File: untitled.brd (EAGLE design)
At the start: 54.8 x 54.7 mm, 25 parts

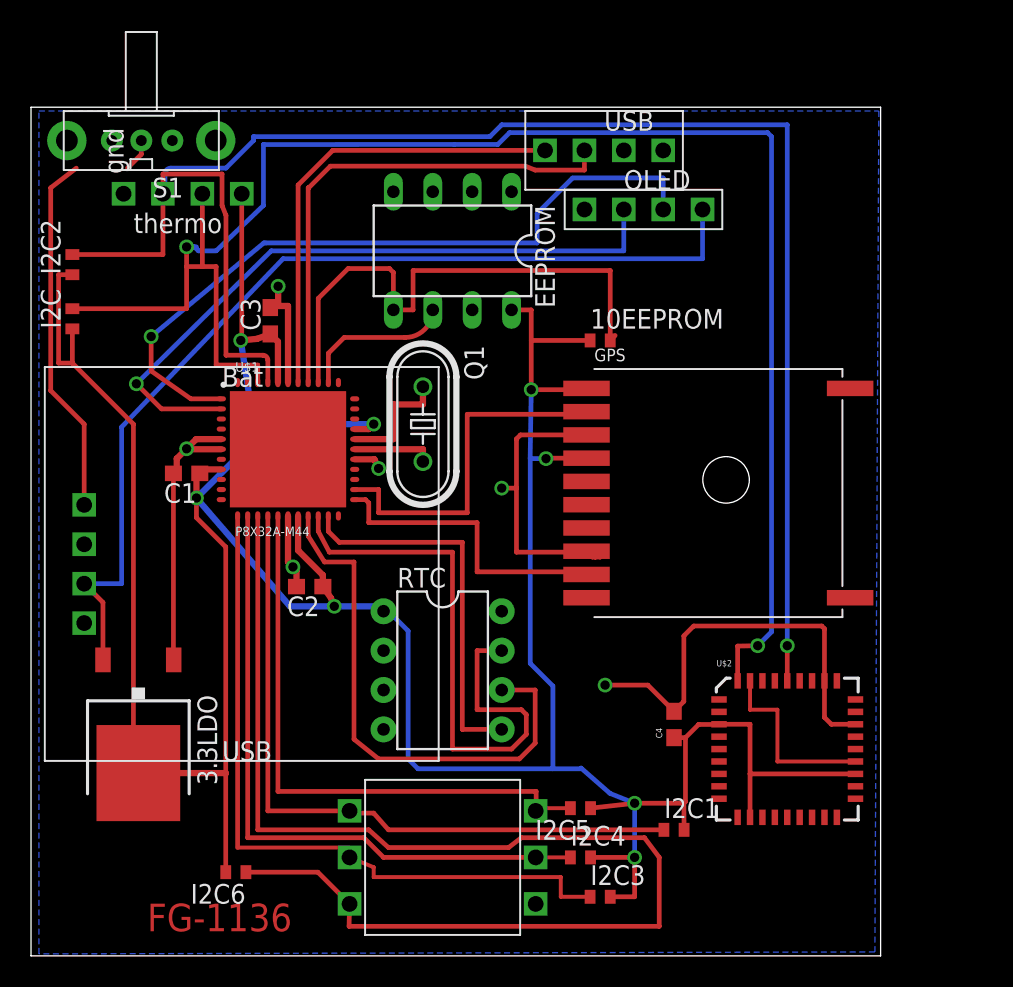
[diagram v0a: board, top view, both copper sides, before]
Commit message: added optional speaker
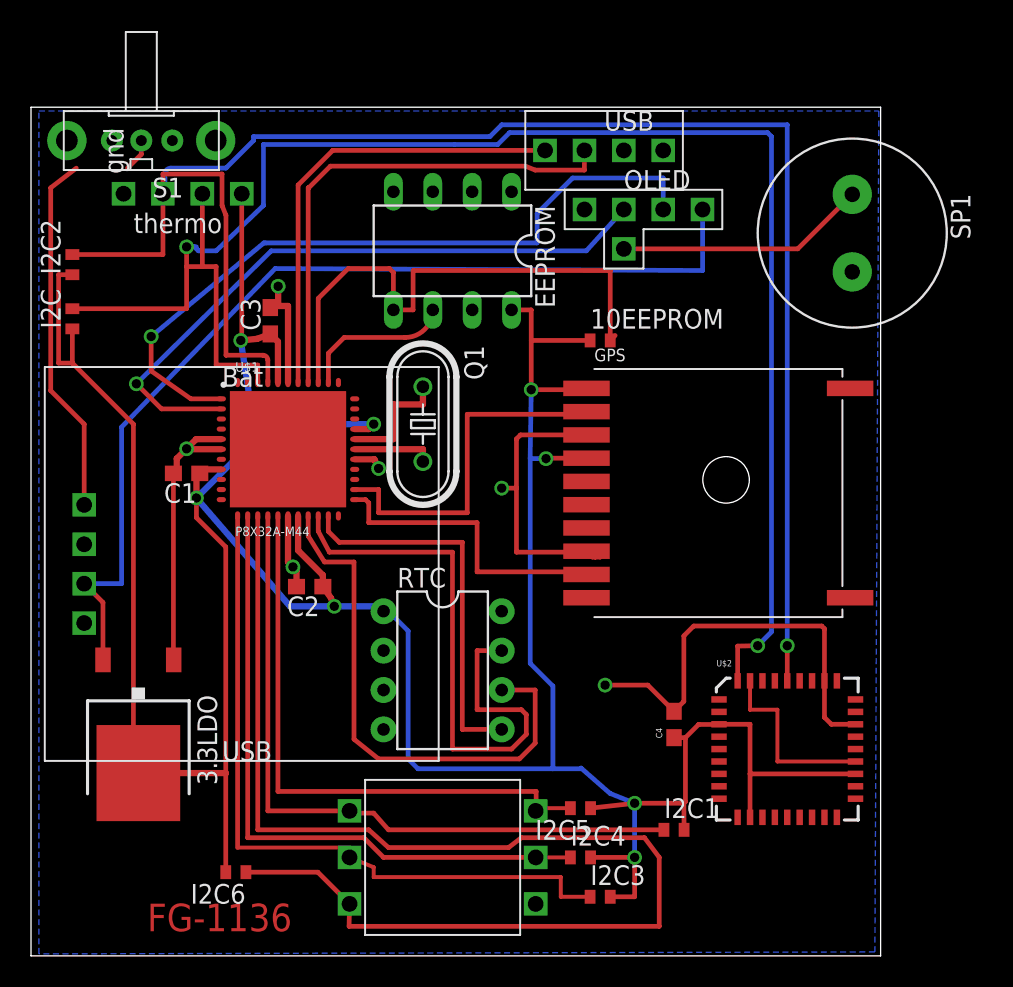
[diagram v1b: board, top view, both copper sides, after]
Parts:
- added SP1: SPEAKER/PS12, adafruit:PS12
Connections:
- new net N$12: OLED_SCREEN.PEZ, SP1.P$1
- net GND: now also SP1.P$2
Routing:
- net N$12: track 0.00 -> 16.2 mm
- net N$10: track 43.8 -> 42.3 mm
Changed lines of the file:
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@@
 <element name="C4" library="SparkFun" package="0603" value="" x="79.6925" y="25.0825" rot="R90"/>
 <element name="3.3LDO" library="burr-brown" package="TO252" value="REG1117X" x="45.1485" y="24.4475" rot="R180"/>
+<element name="SP1" library="adafruit" package="PS12" value="SPEAKER/PS12" x="91.186" y="56.769" rot="R270"/>
 </elements>
 <signals>
@@
 <wire x1="46.6437" y1="45.4313" x2="45.0215" y2="47.0535" width="0.3048" layer="1"/>
 <wire x1="45.0215" y1="47.0535" x2="53.721" y2="55.626" width="0.3048" layer="16"/>
-<wire x1="53.721" y1="55.626" x2="76.454" y2="55.626" width="0.3048" layer="16"/>
-<wire x1="76.454" y1="58.293" x2="76.454" y2="55.626" width="0.3048" layer="16"/>
+<wire x1="53.721" y1="55.626" x2="74.041" y2="55.626" width="0.3048" layer="16"/>
+<wire x1="74.041" y1="55.626" x2="76.454" y2="58.293" width="0.3048" layer="16"/>
 </signal>
 <signal name="N$11">
@@
 <wire x1="47.4285" y1="29.2475" x2="47.41" y2="29.2475" width="0.3048" layer="1"/>
 <wire x1="47.41" y1="29.2475" x2="47.41" y2="41.275" width="0.3048" layer="1"/>
+<contactref element="SP1" pad="P$2"/>
 </signal>
 <signal name="+5V">
@@
 <contactref element="OLED_SCREEN" pad="5V"/>
 <contactref element="3.3LDO" pad="2"/>
-<wire x1="81.534" y1="55.118" x2="54.483" y2="55.118" width="0.3048" layer="16"/>
+<wire x1="81.534" y1="54.356" x2="53.975" y2="54.483" width="0.3048" layer="16"/>
 <wire x1="41.656" y1="34.163" x2="42.8685" y2="32.9505" width="0.3048" layer="1"/>
 <wire x1="42.8685" y1="32.9505" x2="42.8685" y2="29.2475" width="0.3048" layer="1"/>
 <wire x1="44.069" y1="44.2595" x2="44.069" y2="34.163" width="0.3048" layer="16"/>
 <wire x1="44.069" y1="34.163" x2="41.656" y2="34.163" width="0.3048" layer="16"/>
-<wire x1="81.534" y1="58.293" x2="81.534" y2="55.118" width="0.3048" layer="16"/>
-<wire x1="54.483" y1="55.118" x2="44.069" y2="44.2595" width="0.3048" layer="16"/>
+<wire x1="81.534" y1="58.293" x2="81.534" y2="54.356" width="0.3048" layer="16"/>
+<wire x1="53.975" y1="54.483" x2="44.069" y2="44.2595" width="0.3048" layer="16"/>
 </signal>
 <signal name="+3V3">
@@
 <wire x1="70.485" y1="51.816" x2="70.485" y2="49.8475" width="0.3048" layer="1"/>
 </signal>
+<signal name="N$12">
+<contactref element="OLED_SCREEN" pad="PEZ"/>
+<contactref element="SP1" pad="P$1"/>
+<wire x1="91.186" y1="59.269" x2="87.67" y2="55.753" width="0.3048" layer="1"/>
+<wire x1="87.67" y1="55.753" x2="76.454" y2="55.753" width="0.3048" layer="1"/>
+</signal>
 </signals>

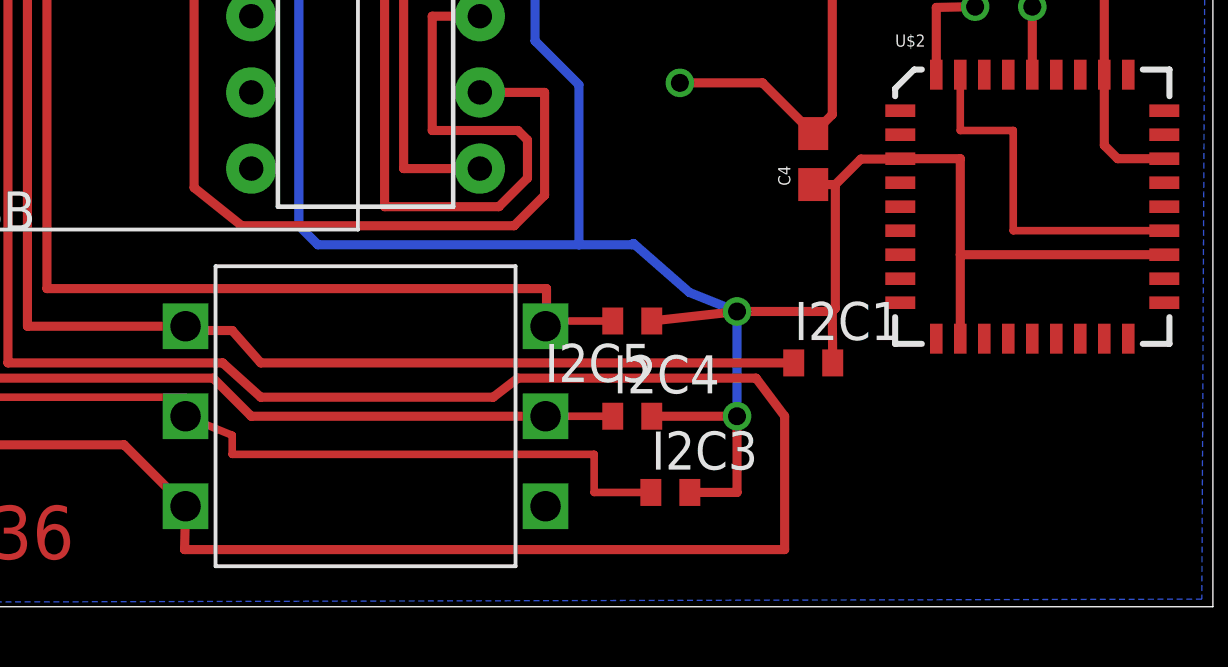
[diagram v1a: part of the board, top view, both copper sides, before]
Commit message: moved switch resistors to better fit 3d case.
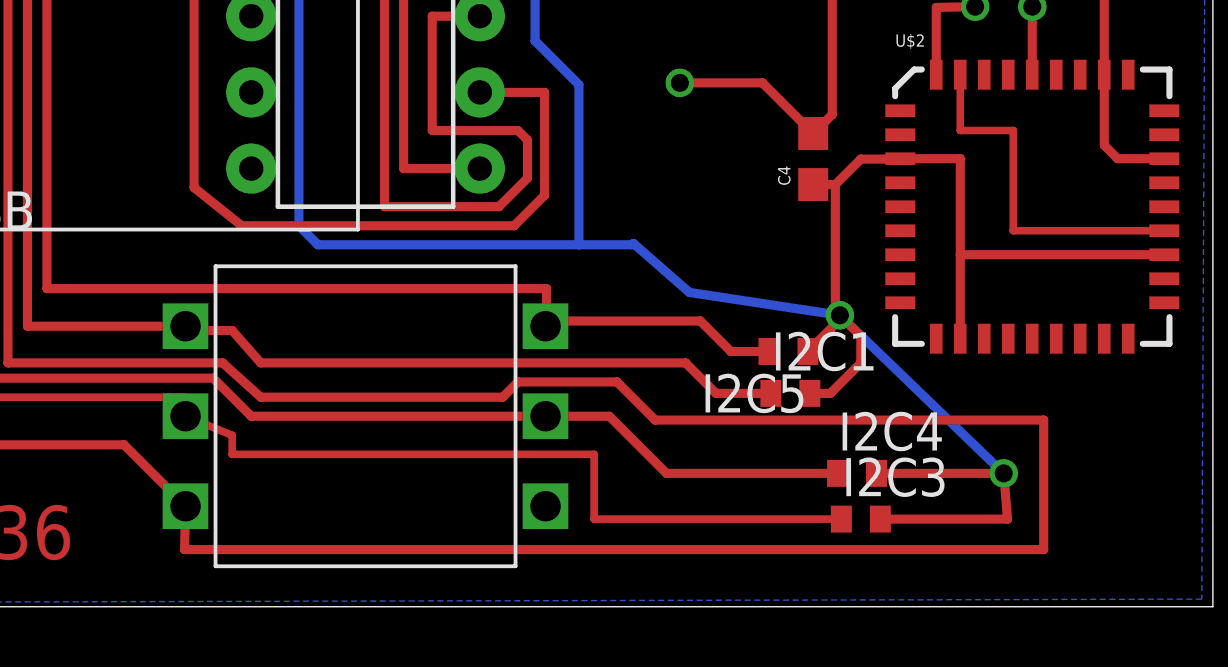
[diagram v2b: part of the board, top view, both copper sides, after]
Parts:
- moved I2C4 7.73 mm to (81.2, 14.6)
- moved I2C3 6.41 mm to (81.3, 13.1)
- moved I2C5 5.31 mm to (78.9, 18.7)
- moved I2C1 1.27 mm to (78.9, 17.3)
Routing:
- net N$15: track 80.8 -> 97.9 mm
- net +3V3: track 238.8 -> 247.4 mm
- net N$20: track 42.1 -> 50.4 mm
- net N$17: track 46.8 -> 54.0 mm
- net N$21: track 38.1 -> 43.7 mm
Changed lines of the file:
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@@
 <element name="I2C2" library="adafruit" package="R1005" value="" x="40.894" y="54.737" rot="R90"/>
 <element name="I2C" library="adafruit" package="R1005" value="" x="40.894" y="51.2445" rot="R90"/>
-<element name="I2C5" library="adafruit" package="R1005" value="" x="73.66" y="19.685" rot="R180"/>
-<element name="I2C4" library="adafruit" package="R1005" value="" x="73.66" y="16.51"/>
-<element name="I2C3" library="adafruit" package="R1005" value="" x="74.93" y="13.97"/>
+<element name="I2C5" library="adafruit" package="R1005" value="" x="78.867" y="18.669" rot="R180"/>
+<element name="I2C4" library="adafruit" package="R1005" value="" x="81.153" y="14.605"/>
+<element name="I2C3" library="adafruit" package="R1005" value="" x="81.28" y="13.081"/>
 <element name="I2C6" library="adafruit" package="R1005" value="" x="51.435" y="15.5575" rot="R180"/>
-<element name="I2C1" library="adafruit" package="R1005" value="" x="79.6925" y="18.288"/>
+<element name="I2C1" library="adafruit" package="R1005" value="" x="78.9305" y="17.272"/>
 <element name="U$2" library="SparkFun" package="LCC36" value="HMC6343A" x="86.995" y="23.495"/>
 <element name="C1" library="rcl" package="C0603" value="" x="48.26" y="41.275" rot="R180"/>
@@
 <wire x1="53.5" y1="38.5313" x2="53.5" y2="19.51" width="0.3048" layer="1"/>
 <wire x1="53.5" y1="19.51" x2="58.77" y2="19.51" width="0.3048" layer="1"/>
-<wire x1="79.0425" y1="18.288" x2="61.2775" y2="18.288" width="0.3048" layer="1"/>
 <wire x1="61.2775" y1="18.288" x2="60.325" y2="19.3675" width="0.3048" layer="1"/>
 <wire x1="60.325" y1="19.3675" x2="58.9125" y2="19.3675" width="0.3048" layer="1"/>
 <wire x1="58.9125" y1="19.3675" x2="58.77" y2="19.51" width="0.3048" layer="1"/>
+<wire x1="78.2805" y1="17.272" x2="76.454" y2="17.272" width="0.3048" layer="1"/>
+<wire x1="75.438" y1="18.288" x2="61.2775" y2="18.288" width="0.3048" layer="1"/>
+<wire x1="75.438" y1="18.288" x2="76.454" y2="17.272" width="0.3048" layer="1"/>
 </signal>
 <signal name="N$15">
@@
 <contactref element="I2C6" pad="1"/>
 <wire x1="52.85" y1="38.5313" x2="52.85" y2="18.288" width="0.3048" layer="1"/>
-<wire x1="77.7875" y1="17.78" x2="78.74" y2="16.51" width="0.3048" layer="1"/>
-<wire x1="78.74" y1="16.51" x2="78.74" y2="12.065" width="0.3048" layer="1"/>
-<wire x1="78.74" y1="12.065" x2="58.7375" y2="12.065" width="0.3048" layer="1"/>
+<wire x1="87.376" y1="16.383" x2="87.376" y2="12.065" width="0.3048" layer="1"/>
+<wire x1="87.376" y1="12.065" x2="58.7375" y2="12.065" width="0.3048" layer="1"/>
 <wire x1="58.7375" y1="12.065" x2="58.77" y2="13.51" width="0.3048" layer="1"/>
 <wire x1="52.85" y1="18.288" x2="60.0075" y2="18.288" width="0.3048" layer="1"/>
 <wire x1="60.0075" y1="18.288" x2="61.2775" y2="17.145" width="0.3048" layer="1"/>
-<wire x1="61.2775" y1="17.145" x2="69.0245" y2="17.145" width="0.3048" layer="1"/>
-<wire x1="69.85" y1="17.78" x2="77.7875" y2="17.78" width="0.3048" layer="1"/>
 <wire x1="52.085" y1="15.5575" x2="56.7225" y2="15.5575" width="0.3048" layer="1"/>
 <wire x1="56.7225" y1="15.5575" x2="58.77" y2="13.51" width="0.3048" layer="1"/>
-<wire x1="69.85" y1="17.78" x2="69.0245" y2="17.145" width="0.3048" layer="1"/>
+<wire x1="61.2775" y1="17.145" x2="69.342" y2="17.145" width="0.3048" layer="1"/>
+<wire x1="69.342" y1="17.145" x2="69.85" y2="17.653" width="0.3048" layer="1"/>
+<wire x1="69.85" y1="17.653" x2="73.152" y2="17.653" width="0.3048" layer="1"/>
+<wire x1="74.422" y1="16.383" x2="87.376" y2="16.383" width="0.3048" layer="1"/>
+<wire x1="73.152" y1="17.653" x2="74.422" y2="16.383" width="0.3048" layer="1"/>
 </signal>
 <signal name="N$17">
@@
 <contactref element="U$1" pad="12"/>
 <contactref element="5WAYSWITCH" pad="L"/>
-<wire x1="74.28" y1="13.97" x2="72.39" y2="13.97" width="0.254" layer="1"/>
-<wire x1="72.39" y1="13.97" x2="72.39" y2="15.24" width="0.254" layer="1"/>
+<wire x1="80.63" y1="13.081" x2="72.39" y2="13.081" width="0.254" layer="1"/>
+<wire x1="72.39" y1="13.081" x2="72.39" y2="15.24" width="0.254" layer="1"/>
 <wire x1="72.39" y1="15.24" x2="60.325" y2="15.24" width="0.254" layer="1"/>
 <wire x1="60.325" y1="15.24" x2="60.325" y2="15.875" width="0.254" layer="1"/>
@@
 <contactref element="I2C4" pad="1"/>
 <contactref element="U$1" pad="13"/>
-<wire x1="73.01" y1="16.51" x2="70.77" y2="16.51" width="0.254" layer="1"/>
 <wire x1="52.2" y1="38.5313" x2="52.2" y2="17.78" width="0.3048" layer="1"/>
 <wire x1="70.8025" y1="16.51" x2="70.77" y2="16.51" width="0.3048" layer="1"/>
@@
 <wire x1="59.69" y1="17.78" x2="60.96" y2="16.51" width="0.3048" layer="1"/>
 <wire x1="60.96" y1="16.51" x2="70.77" y2="16.51" width="0.3048" layer="1"/>
+<wire x1="74.803" y1="14.605" x2="80.503" y2="14.605" width="0.3048" layer="1"/>
+<wire x1="70.77" y1="16.51" x2="72.898" y2="16.51" width="0.3048" layer="1"/>
+<wire x1="72.898" y1="16.51" x2="74.803" y2="14.605" width="0.3048" layer="1"/>
 </signal>
 <signal name="N$21">
@@
 <contactref element="U$1" pad="16"/>
 <contactref element="I2C5" pad="2"/>
-<wire x1="73.01" y1="19.685" x2="70.77" y2="19.685" width="0.254" layer="1"/>
 <wire x1="70.77" y1="19.685" x2="70.77" y2="19.51" width="0.254" layer="1"/>
 <wire x1="54.15" y1="38.5313" x2="54.15" y2="20.7645" width="0.3048" layer="1"/>
@@
 <wire x1="70.8025" y1="20.7645" x2="70.8025" y2="19.51" width="0.3048" layer="1"/>
 <wire x1="70.8025" y1="19.51" x2="70.77" y2="19.51" width="0.3048" layer="1"/>
+<wire x1="70.77" y1="19.685" x2="75.931" y2="19.685" width="0.3048" layer="1"/>
+<wire x1="75.931" y1="19.685" x2="76.947" y2="18.669" width="0.3048" layer="1"/>
+<wire x1="76.947" y1="18.669" x2="78.217" y2="18.669" width="0.3048" layer="1"/>
 </signal>
 <signal name="N$22">
@@
 <wire x1="60.96" y1="32.7025" x2="57.785" y2="32.7025" width="0.4064" layer="16"/>
 <wire x1="73.6993375" y1="22.26995625" x2="75.565" y2="20.6375" width="0.3048" layer="16"/>
-<wire x1="75.565" y1="20.6375" x2="77.1525" y2="20.0025" width="0.3048" layer="16"/>
-<wire x1="77.1525" y1="20.0025" x2="77.1525" y2="16.51" width="0.3048" layer="16"/>
-<via x="77.1525" y="16.51" extent="1-16" drill="0.6" shape="square"/>
-<wire x1="77.1525" y1="16.51" x2="74.31" y2="16.51" width="0.3048" layer="1"/>
-<via x="77.1525" y="20.0025" extent="1-16" drill="0.6" shape="square"/>
-<wire x1="77.1525" y1="20.0025" x2="74.31" y2="19.685" width="0.3048" layer="1"/>
-<wire x1="75.58" y1="13.97" x2="77.1525" y2="13.97" width="0.3048" layer="1"/>
-<wire x1="77.1525" y1="13.97" x2="77.1525" y2="16.51" width="0.3048" layer="1"/>
-<wire x1="77.1525" y1="20.0025" x2="80.3275" y2="20.0025" width="0.3048" layer="1"/>
-<wire x1="80.3275" y1="20.0025" x2="80.3425" y2="18.288" width="0.3048" layer="1"/>
+<wire x1="75.565" y1="20.6375" x2="80.5815" y2="19.8755" width="0.3048" layer="16"/>
+<wire x1="80.5815" y1="19.8755" x2="86.0425" y2="14.605" width="0.3048" layer="16"/>
+<via x="86.0425" y="14.605" extent="1-16" drill="0.6" shape="square"/>
+<via x="80.5815" y="19.8755" extent="1-16" drill="0.6" shape="square"/>
+<wire x1="81.93" y1="13.081" x2="86.1695" y2="13.081" width="0.3048" layer="1"/>
+<wire x1="86.1695" y1="13.081" x2="86.0425" y2="14.605" width="0.3048" layer="1"/>
 <wire x1="50.785" y1="15.5575" x2="50.785" y2="21.9075" width="0.3048" layer="1"/>
 <wire x1="50.785" y1="21.9475" x2="50.785" y2="36.5275" width="0.3048" layer="1"/>
@@
 <wire x1="81.28" y1="25.0825" x2="82.5825" y2="25.0825" width="0.3048" layer="1"/>
 <wire x1="82.5825" y1="25.0825" x2="82.595" y2="25.095" width="0.3048" layer="1"/>
-<wire x1="80.43" y1="24.2325" x2="80.43" y2="20.105" width="0.3048" layer="1"/>
-<wire x1="80.43" y1="20.105" x2="80.3275" y2="20.0025" width="0.3048" layer="1"/>
 <contactref element="GPS" pad="P$4"/>
 <wire x1="74.05" y1="42.255" x2="71.465" y2="42.255" width="0.3048" layer="1"/>
@@
 <wire x1="69.215" y1="51.816" x2="70.485" y2="51.816" width="0.3048" layer="1"/>
 <wire x1="70.485" y1="51.816" x2="70.485" y2="49.8475" width="0.3048" layer="1"/>
+<wire x1="81.803" y1="14.605" x2="86.0425" y2="14.605" width="0.3048" layer="1"/>
+<wire x1="80.5815" y1="19.8755" x2="80.43" y2="20.027" width="0.3048" layer="1"/>
+<wire x1="80.43" y1="20.027" x2="80.43" y2="24.2325" width="0.3048" layer="1"/>
+<wire x1="79.517" y1="18.669" x2="80.5815" y2="19.7335" width="0.3048" layer="1"/>
+<wire x1="80.5815" y1="19.7335" x2="80.5815" y2="19.8755" width="0.3048" layer="1"/>
+<wire x1="79.5805" y1="17.272" x2="80.264" y2="17.272" width="0.3048" layer="1"/>
+<wire x1="80.264" y1="17.272" x2="81.28" y2="18.288" width="0.3048" layer="1"/>
+<wire x1="81.28" y1="18.288" x2="81.28" y2="19.177" width="0.3048" layer="1"/>
+<wire x1="81.28" y1="19.177" x2="80.5815" y2="19.8755" width="0.3048" layer="1"/>
 </signal>
 <signal name="N$12">
